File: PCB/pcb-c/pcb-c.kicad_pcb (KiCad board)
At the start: 2 copper layers, 60.5 x 35.5 mm, 41 parts, among them Q1 BC817, Q13 TPCA8120,L1Q, Q2 TPCA8120,L1Q, Q3 BC817, Q4 BC817, Q5 TPCA8120,L1Q, Q6 BC817, Q7 TPCA8120,L1Q, Q8 BC817, Q9 TPCA8120,L1Q

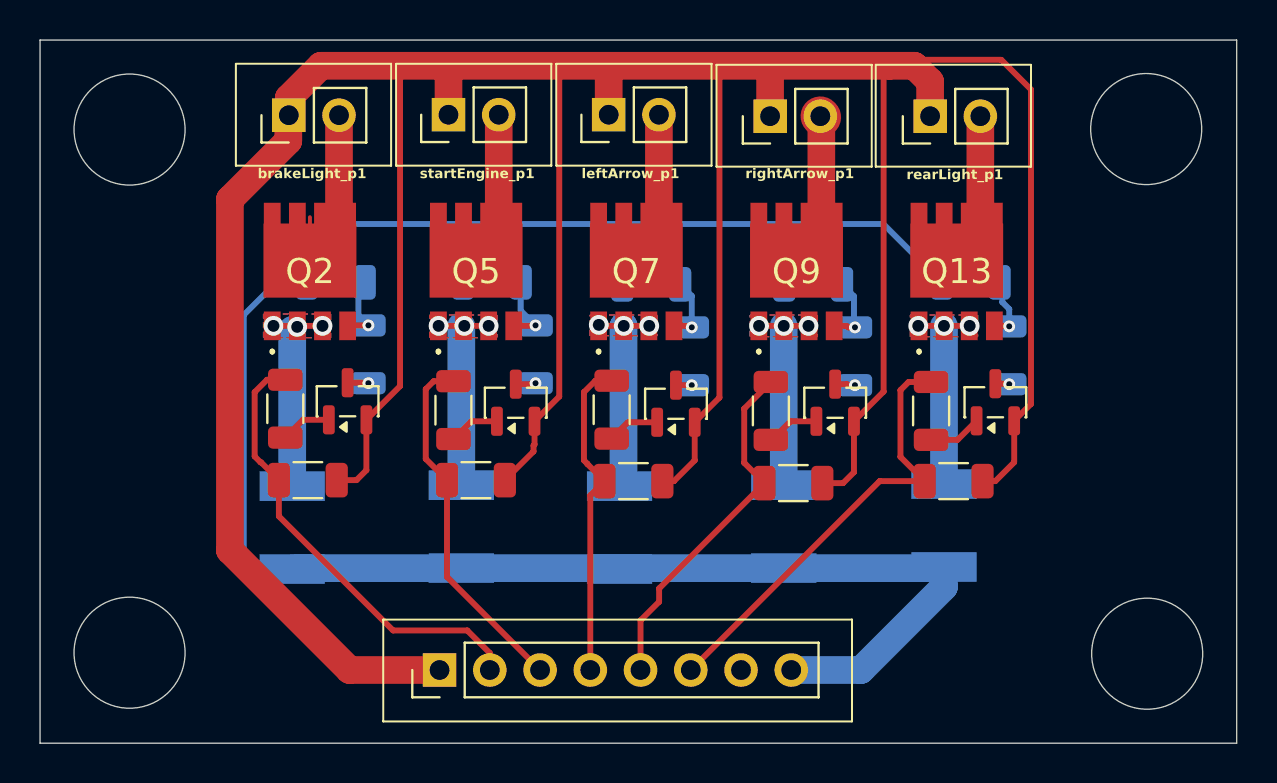
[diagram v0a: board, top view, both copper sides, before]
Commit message: Size reducing (48.3mm x 34.5mm)
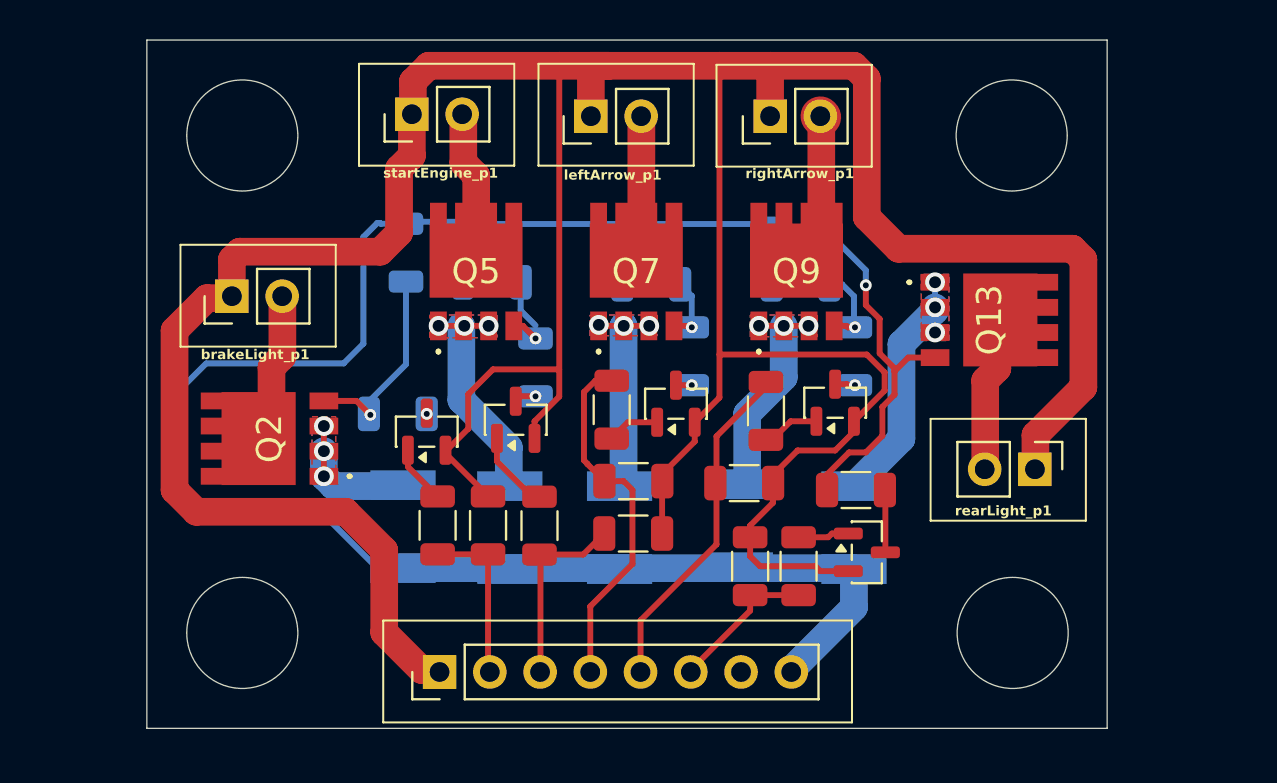
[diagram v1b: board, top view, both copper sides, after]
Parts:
- R3: moved to F.Cu
- moved rearLight_p1 18.6 mm to (195.2, 108.2), turned to -90 degrees
- moved R21 11.2 mm to (180.8, 113.0), turned to -90 degrees
- moved R7 10.3 mm to (183.2, 113.0), turned to -90 degrees
- moved R3 10.3 mm to (186.1, 109.2), turned to 180 degrees
- moved Q3 9.99 mm to (186.7, 112.3), turned to 0 degrees
- moved R4 9.70 mm to (164.9, 111.0), turned to -90 degrees
- moved brakeLight_p1 9.59 mm to (154.6, 99.4)
- moved R1 9.40 mm to (167.5, 111.0), turned to -90 degrees
- moved R2 8.94 mm to (183.3, 96.2)
- moved Q2 8.69 mm to (156.4, 106.6), turned to 90 degrees
- moved R8 8.40 mm to (174.8, 111.4)
- moved R9 7.28 mm to (170.1, 111.0), turned to -90 degrees
- moved F2 5.60 mm to (163.2, 111.0)
- moved F3 4.55 mm to (186.0, 111.1)
- moved Q1 4.29 mm to (164.4, 106.2)
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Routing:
- net Net-(Q13-G): track 3.19 -> 18.6 mm
- net c_rearLight: track 22.6 -> 7.58 mm
- net c_brakeSwitch: track 23.0 -> 8.54 mm
- net +12V: track 107.1 -> 93.6 mm
- net c_startEngine: track 18.2 -> 9.96 mm
- net Net-(Q2-G): track 3.57 -> 10.1 mm
- net GND: track 198.4 -> 193.3 mm
- net Net-(Q13-S_1): track 10.5 -> 14.5 mm
- net Net-(Q2-D_1): track 10.2 -> 7.70 mm
- net Net-(Q3-C): track 0.71 -> 3.16 mm, vias 1 -> 0
- net Net-(Q2-S_1): track 10.4 -> 8.03 mm
- net c_leftArrow: track 16.4 -> 18.2 mm
- net Net-(Q4-B): track 2.57 -> 4.05 mm
- net Net-(Q5-S_1): track 10.6 -> 11.7 mm
- net Net-(Q1-C): track 1.06 -> 0.00 mm
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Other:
- board size 60.5 x 35.5 mm -> 48.6 x 34.8 mm

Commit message: Rimozione resistenge sui gates e aggiunta diodo fly-back
PCB size reducing
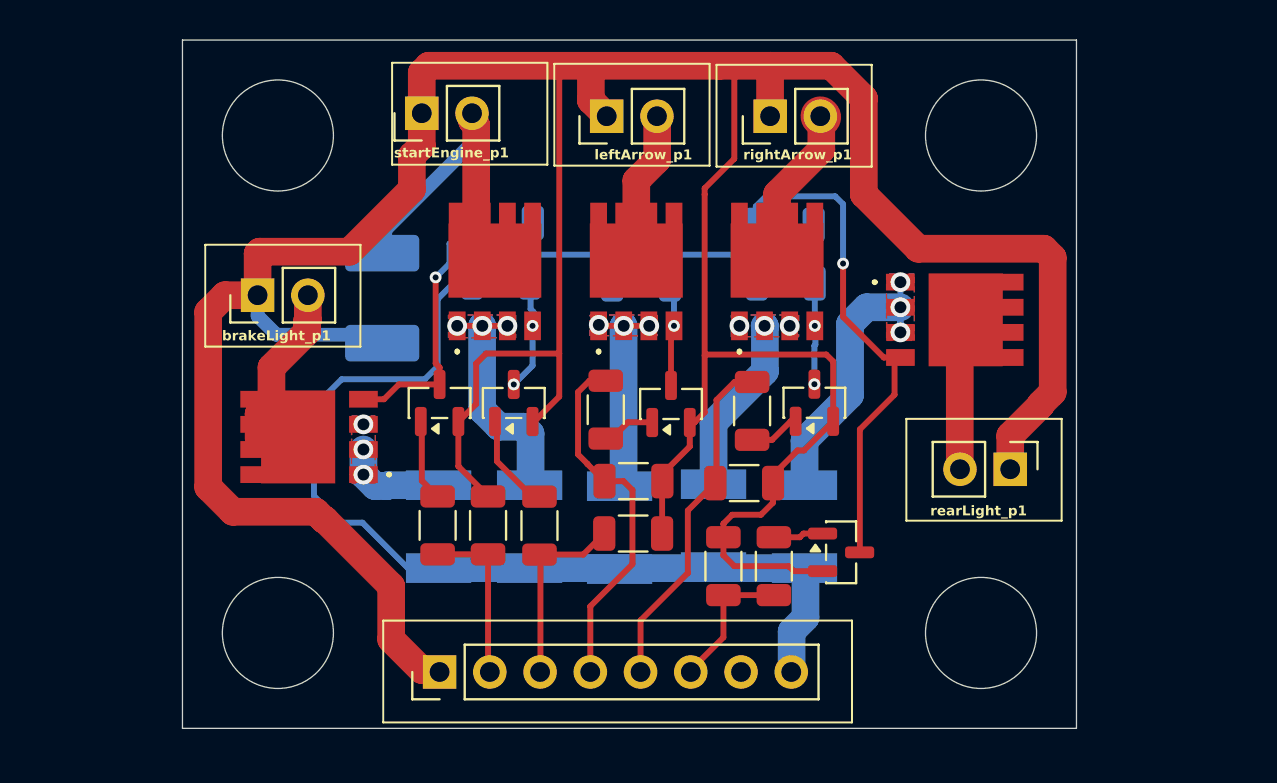
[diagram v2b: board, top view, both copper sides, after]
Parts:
- removed R11, R15, R19, R3, R6: 33K, Resistor_SMD:R_1206_3216Metric
- added D1: D_Small, Diode_SMD:D_2114_3652Metric_Pad1.85x3.75mm_HandSolder, B.Cu at (162.2, 99.5)
- R10, R14, R18, R2, R5: value 10K -> 15K
- moved R5 5.17 mm to (168.3, 95.7), turned to 180 degrees
- moved F3 2.50 mm to (183.5, 111.0)
- moved Q2 2.00 mm to (158.4, 106.5)
- moved F2 1.80 mm to (165.0, 111.0)
- moved Q13 1.75 mm to (191.1, 100.6)
- moved Q1 1.59 mm to (165.1, 104.8)
- moved F1 1.35 mm to (178.9, 111.0)
- moved R21 1.35 mm to (179.4, 113.0)
- moved brakeLight_p1 1.30 mm to (155.8, 99.3)
- moved Q3 1.30 mm to (185.3, 112.3)
- moved R7 1.25 mm to (181.9, 113.0)
- moved rearLight_p1 1.25 mm to (193.9, 108.2)
- moved Q8 1.05 mm to (184.0, 104.8)
- moved F5 1.00 mm to (169.6, 111.0)
- moved Q9 0.98 mm to (182.1, 98.2)
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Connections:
- Q2 pad 4: Net-(Q2-G) -> Net-(Q1-C)
- Q3 pad 3: Net-(Q3-C) -> Net-(Q13-G)
- Q5 pad 4: Net-(Q5-G) -> Net-(Q4-C)
- Q7 pad 4: Net-(Q7-G) -> Net-(Q6-C)
- Q9 pad 4: Net-(Q9-G) -> Net-(Q8-C)
- R10 pad 1: Net-(Q5-G) -> +12V
- R10 pad 2: +12V -> Net-(Q4-C)
- R14 pad 1: Net-(Q7-G) -> +12V
- R14 pad 2: +12V -> Net-(Q6-C)
- R18 pad 1: Net-(Q9-G) -> +12V
- R18 pad 2: +12V -> Net-(Q8-C)
- R2 pad 1: Net-(Q13-G) -> +12V
- R2 pad 2: +12V -> Net-(Q13-G)
- R5 pad 1: Net-(Q2-G) -> +12V
- R5 pad 2: +12V -> Net-(Q1-C)
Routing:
- net +12V: track 93.6 -> 74.4 mm
- net Net-(Q1-C): track 0.00 -> 13.4 mm
- net Net-(Q2-G): track 10.1 -> 0.00 mm, vias 1 -> 0
- net Net-(D1-K): track 7.70 -> 16.5 mm
- net Net-(Q13-G): track 18.6 -> 26.7 mm
- net Net-(Q4-C): track 1.10 -> 5.80 mm, vias 1 -> 2
- net Net-(Q6-C): track 0.80 -> 5.26 mm
- net Net-(Q9-G): track 4.16 -> 0.00 mm, vias 1 -> 0
- net Net-(Q8-C): track 1.02 -> 5.14 mm, vias 1 -> 2
- net Net-(Q5-G): track 3.85 -> 0.00 mm, vias 1 -> 0
- net Net-(Q7-G): track 3.35 -> 0.00 mm, vias 1 -> 0
- net Net-(Q3-C): track 3.16 -> 0.00 mm
- net Net-(Q2-S_1): track 8.03 -> 5.33 mm
- net Net-(Q9-S_1): track 11.5 -> 9.09 mm
- net GND: track 193.3 -> 191.3 mm
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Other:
- board size 48.6 x 34.8 mm -> 45.2 x 34.8 mm

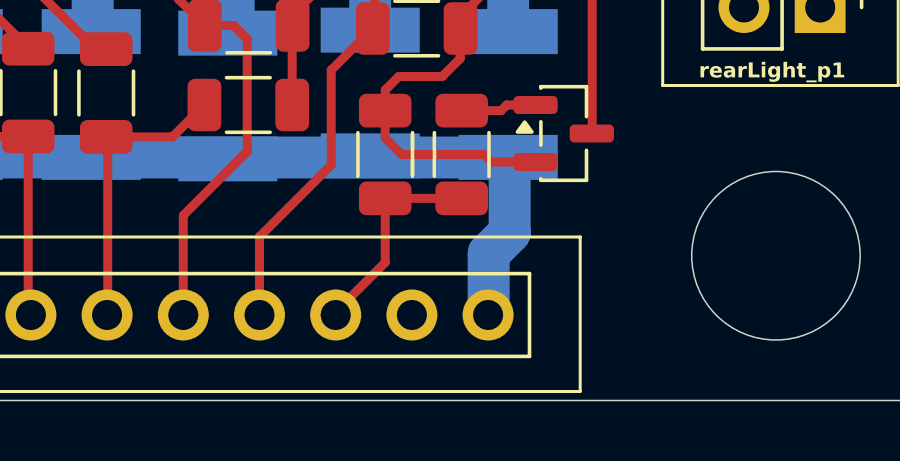
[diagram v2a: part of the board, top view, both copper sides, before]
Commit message: High current on 2.54 pin-header connector pin 8 fixed
- All electric currect flowed trough the pin 8. Every pin should allows 2A max, so it could be morked in critical area.
  So, due to I am paranoide, I connected the unused pin 7 to the 8.
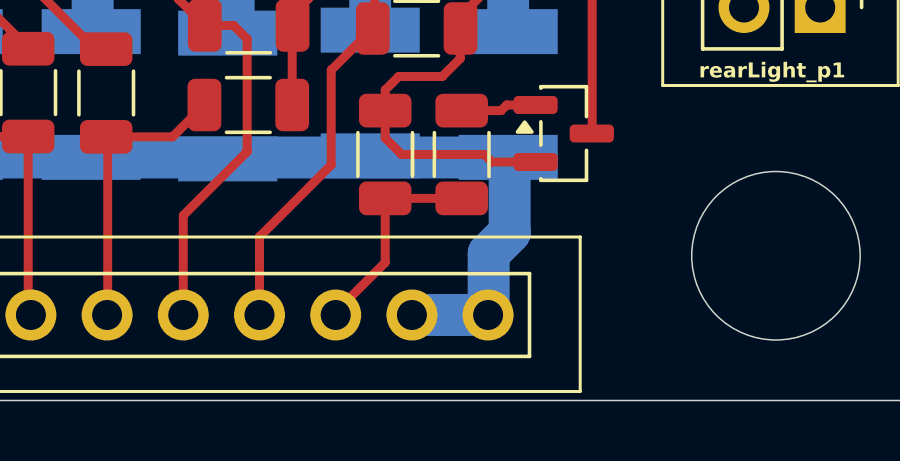
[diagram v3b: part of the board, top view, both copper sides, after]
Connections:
- RearDevs1 pad 7: unconnected-(RearDevs1-Pin_7-Pad7) -> +12V
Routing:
- net +12V: track 74.4 -> 77.0 mm
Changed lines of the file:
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@@
 	(net 25 "Net-(Q8-B)")
 	(net 26 "Net-(Q8-C)")
-	(net 27 "unconnected-(RearDevs1-Pin_7-Pad7)")
-	(net 28 "c_startEngine")
+	(net 27 "c_startEngine")
 	(footprint "Resistor_SMD:R_1206_3216Metric"
 		(layer "F.Cu")
@@
 			(layers "F.Cu" "F.Mask" "F.Paste")
 			(roundrect_rratio 0.222222)
-			(net 28 "c_startEngine")
+			(net 27 "c_startEngine")
 			(pintype "passive")
 		)
@@
 			(layers "*.Cu" "*.Mask")
 			(remove_unused_layers no)
-			(net 28 "c_startEngine")
+			(net 27 "c_startEngine")
 			(pinfunction "Pin_3")
 			(pintype "passive")
@@
 			(layers "*.Cu" "*.Mask")
 			(remove_unused_layers no)
-			(net 27 "unconnected-(RearDevs1-Pin_7-Pad7)")
+			(net 12 "+12V")
 			(pinfunction "Pin_7")
-			(pintype "passive+no_connect")
+			(pintype "passive")
 		)
 		(pad "8" thru_hole circle
@@
 			(layers "F.Cu" "F.Mask" "F.Paste")
 			(roundrect_rratio 0.222222)
-			(net 28 "c_startEngine")
+			(net 27 "c_startEngine")
 			(pintype "passive")
 		)
@@
 	)
 	(segment
+		(start 182.83 118.4)
+		(end 180.29 118.4)
+		(width 1.4)
+		(layer "B.Cu")
+		(net 12)
+	)
+	(segment
 		(start 183.55 115.65)
 		(end 183.55 113.1955)
@@
 		(width 0.3)
 		(layer "F.Cu")
-		(net 28)
+		(net 27)
 	)
 	(segment
@@
 		(width 0.3)
 		(layer "F.Cu")
-		(net 28)
+		(net 27)
 	)
 	(segment
@@
 		(width 0.3)
 		(layer "F.Cu")
-		(net 28)
+		(net 27)
 	)
 	(segment
@@
 		(width 0.3)
 		(layer "F.Cu")
-		(net 28)
+		(net 27)
 	)
 	(segment
@@
 		(width 0.3)
 		(layer "F.Cu")
-		(net 28)
+		(net 27)
 	)
 	(segment
@@
 		(width 0.3)
 		(layer "F.Cu")
-		(net 28)
+		(net 27)
 	)
 	(segment
@@
 		(width 0.3)
 		(layer "F.Cu")
-		(net 28)
+		(net 27)
 	)
 	(segment
@@
 		(width 0.3)
 		(layer "F.Cu")
-		(net 28)
+		(net 27)
 	)
 	(zone

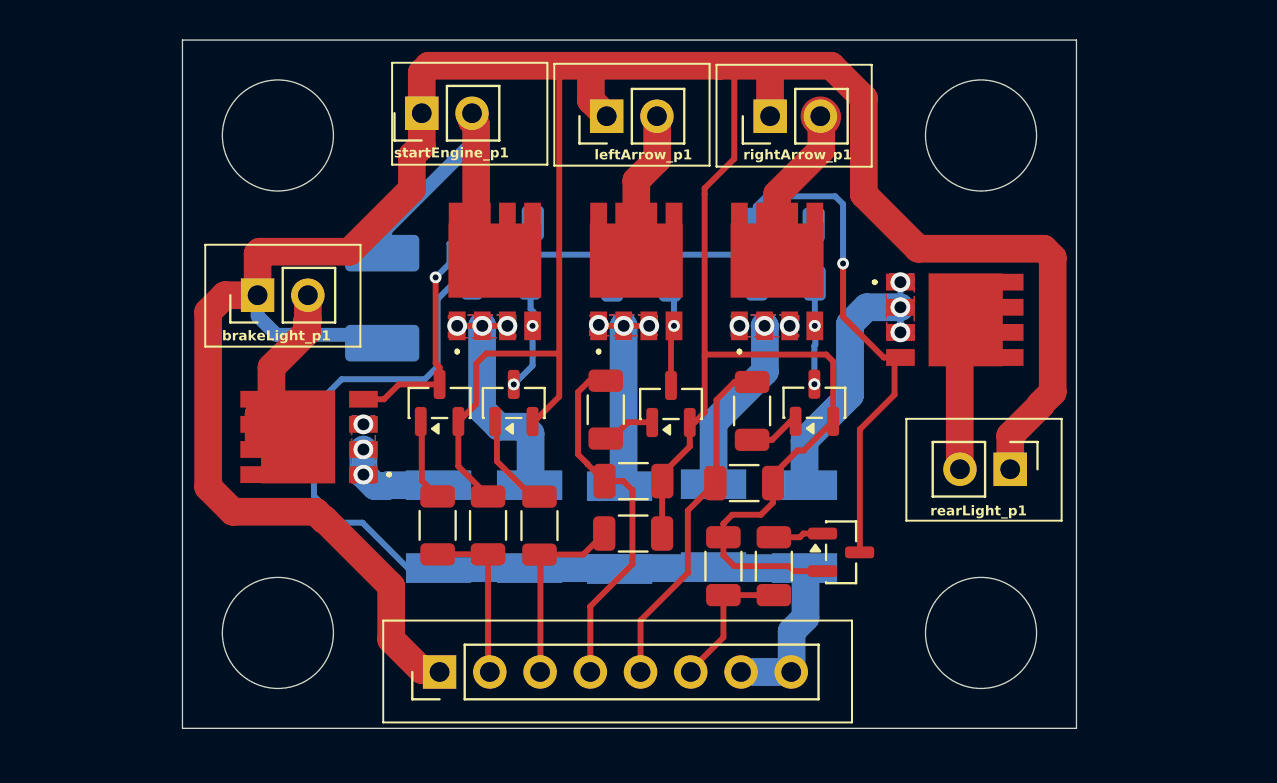
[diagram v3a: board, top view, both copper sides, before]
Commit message: RevDev connector has been changed from 8x1 to 5x2 pins
In order to dedicate two pins to GND too, I have used a 10 pins connector
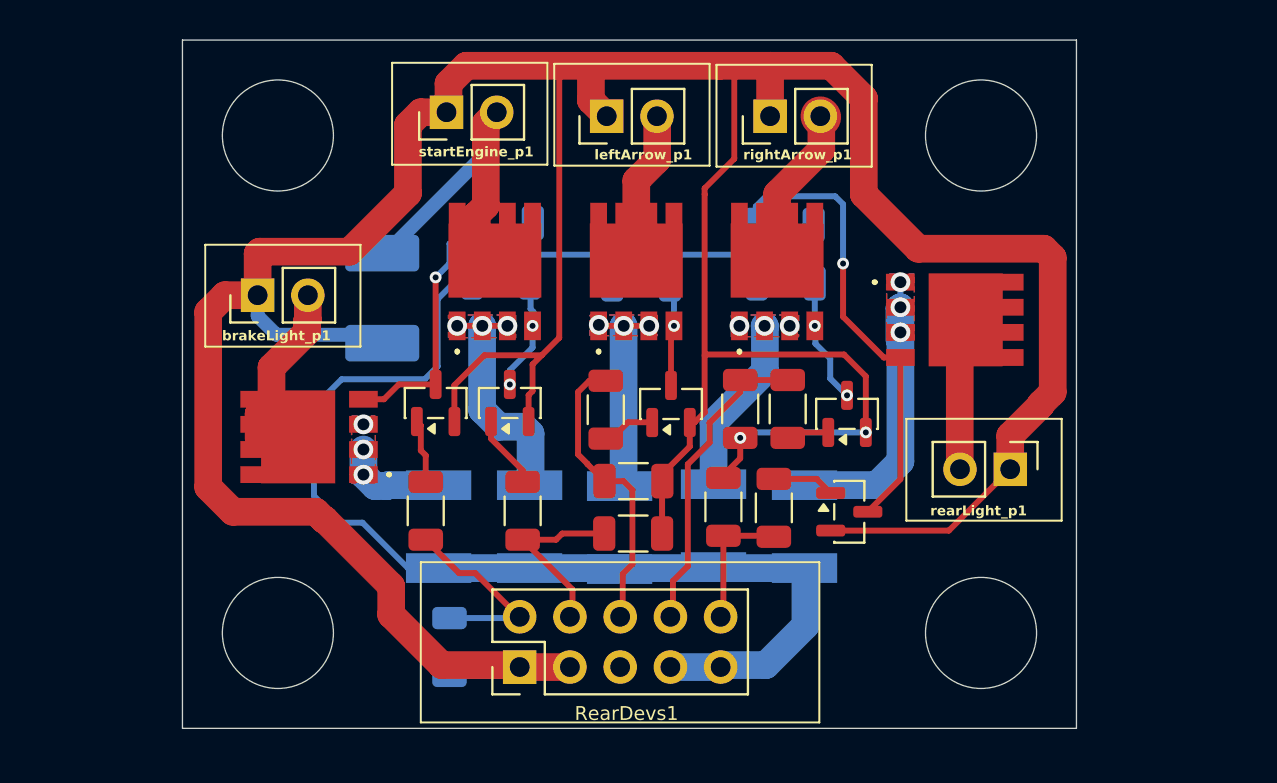
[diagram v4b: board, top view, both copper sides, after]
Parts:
- R1: moved to B.Cu
- RearDevs1: value Conn_01x08 -> Conn_01x10; footprint Connector_PinHeader_2.54mm:PinHeader_1x08_P2.54mm_Vertical -> Connector_PinHeader_2.54mm:PinHeader_2x05_P2.54mm_Vertical
- moved R1 6.45 mm to (165.6, 117.1), turned to 90 degrees
- moved RearDevs1 4.06 mm to (169.1, 118.2)
- moved R16 3.76 mm to (180.2, 105.1), turned to 90 degrees
- moved R21 3.00 mm to (179.4, 110.0)
- moved R7 2.95 mm to (181.9, 110.1)
- moved Q3 2.09 mm to (185.8, 110.3)
- moved R17 1.80 mm to (182.7, 105.1)
- moved Q8 1.74 mm to (185.7, 105.3)
- moved startEngine_p1 1.25 mm to (165.4, 90.1)
- moved R9 1.13 mm to (169.2, 110.2)
- moved R4 0.95 mm to (164.3, 110.2)
- moved Q1 0.20 mm to (164.8, 104.8)
- moved Q4 0.20 mm to (168.6, 104.8)
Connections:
- RearDevs1 pad 3: c_startEngine -> GND
- RearDevs1 pad 4: c_leftArrow -> c_startEngine
- RearDevs1 pad 5: c_rightArrow -> unconnected-(RearDevs1-Pin_5-Pad5)
- RearDevs1 pad 6: c_rearLight -> c_leftArrow
- RearDevs1 pad 8: +12V -> c_rightArrow
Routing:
- net GND: track 191.3 -> 200.7 mm, vias 0 -> 2
- net c_leftArrow: track 18.4 -> 15.0 mm
- net Net-(Q13-S_1): track 15.8 -> 18.6 mm
- net +12V: track 77.0 -> 79.5 mm
- net Net-(Q13-G): track 26.7 -> 24.5 mm
- net c_brakeSwitch: track 8.54 -> 10.1 mm
- net c_rightArrow: track 17.5 -> 16.2 mm
- net Net-(D1-K): track 16.5 -> 17.8 mm
- net Net-(Q4-B): track 4.94 -> 3.71 mm
- net Net-(Q8-C): track 5.14 -> 6.34 mm
- net Net-(Q1-B): track 4.14 -> 3.24 mm
- net c_startEngine: track 9.96 -> 9.25 mm
- net Net-(Q3-B): track 2.54 -> 3.17 mm

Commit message: Mesge from ESP32__dualPCB
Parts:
- added R11: 100K, Resistor_SMD:R_1206_3216Metric, B.Cu at (178.6, 97.3)
- added R15: 100K, Resistor_SMD:R_1206_3216Metric, B.Cu at (173.6, 97.3)
- added R19: 100K, Resistor_SMD:R_1206_3216Metric, B.Cu at (189.8, 100.0)
- added R3: 100K, Resistor_SMD:R_1206_3216Metric, B.Cu at (172.1, 105.1)
- added R6: 100K, Resistor_SMD:R_1206_3216Metric, B.Cu at (159.8, 107.3)
- D1: value D_Small -> M7
- R13, R17, R4, R7, R9: value 10K -> 15K
- moved R14 1.73 mm to (176.1, 97.3), turned to -90 degrees
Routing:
- net +12V: track 79.5 -> 95.8 mm
- net Net-(Q13-S_1): track 18.6 -> 14.4 mm
- net Net-(Q5-S_1): track 12.4 -> 15.8 mm
- net Net-(Q9-S_1): track 9.09 -> 11.9 mm
- net Net-(Q7-S_1): track 10.7 -> 13.0 mm
